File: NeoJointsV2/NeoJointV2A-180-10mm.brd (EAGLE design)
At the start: 30.5 x 12.4 mm, 5 parts

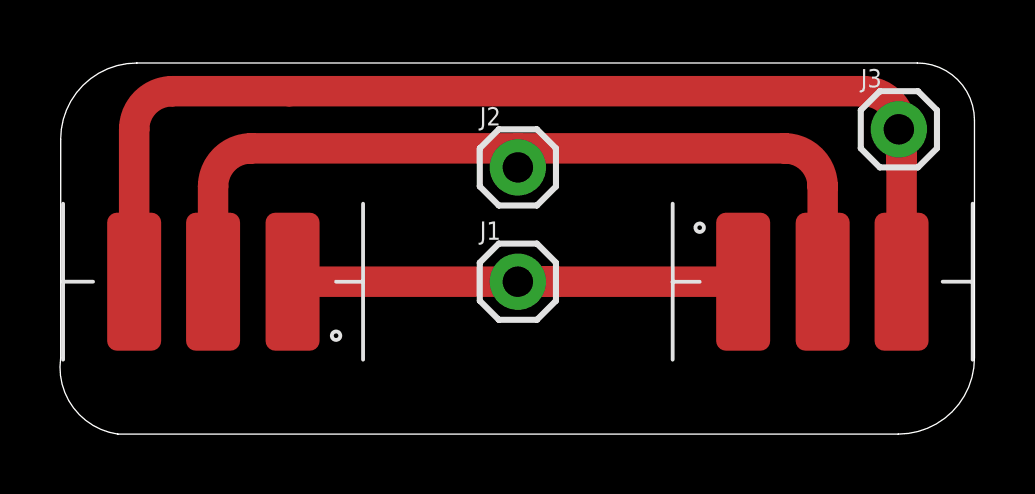
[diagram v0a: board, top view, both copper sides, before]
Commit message: added 180-degree variants
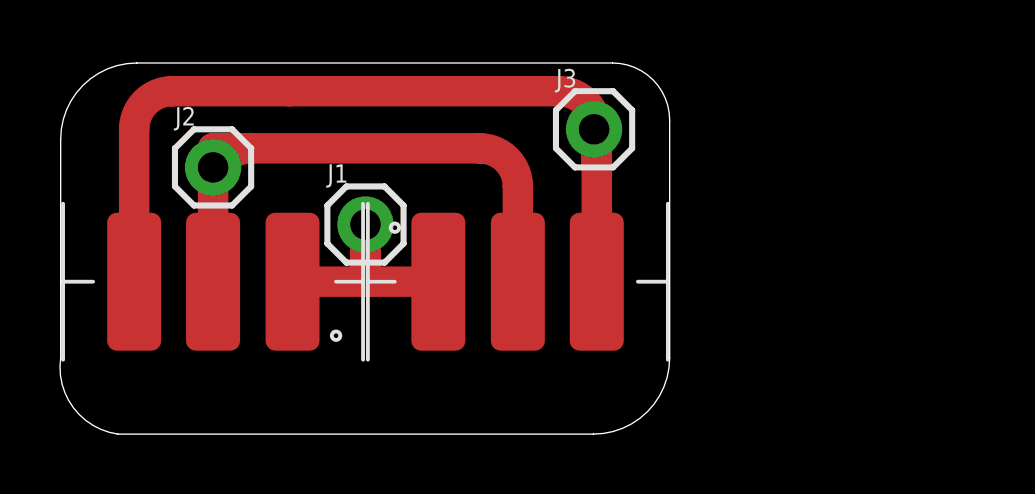
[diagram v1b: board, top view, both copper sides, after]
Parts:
- moved J2 10.2 mm to (5.08, 8.89)
- moved J3 10.2 mm to (17.8, 10.2)
- moved U$2 10.2 mm to (15.2, 5.08)
- moved J1 5.43 mm to (10.2, 6.99)
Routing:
- net N$3: track 38.1 -> 27.9 mm
- net N$1: track 16.3 -> 8.67 mm
- net N$2: track 28.4 -> 20.7 mm
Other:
- board size 30.5 x 12.4 mm -> 20.3 x 12.4 mm
- board text added: "J1"
- board text added: "J2"
- board text added: "J3"
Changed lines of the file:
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@@
 <layer number="123" name="tTestmark" color="7" fill="1" visible="no" active="yes"/>
 <layer number="124" name="bTestmark" color="7" fill="1" visible="no" active="yes"/>
-<layer number="125" name="_tNames" color="7" fill="1" visible="yes" active="yes"/>
+<layer number="125" name="_tNames" color="14" fill="1" visible="yes" active="yes"/>
 <layer number="126" name="_bNames" color="7" fill="1" visible="yes" active="yes"/>
 <layer number="127" name="_tValues" color="7" fill="1" visible="yes" active="yes"/>
@@
 <wire x1="0" y1="9.83" x2="0" y2="2.54" width="0" layer="20"/>
 <wire x1="0" y1="2.54" x2="1.905" y2="0" width="0" layer="20" curve="90"/>
-<wire x1="1.905" y1="0" x2="27.92" y2="0" width="0" layer="20"/>
-<wire x1="27.92" y1="0" x2="30.46" y2="2.54" width="0" layer="20" curve="90"/>
-<wire x1="30.46" y1="2.54" x2="30.46" y2="10.465" width="0" layer="20"/>
-<wire x1="30.46" y1="10.465" x2="28.555" y2="12.37" width="0" layer="20" curve="90"/>
-<wire x1="28.555" y1="12.37" x2="2.54" y2="12.37" width="0" layer="20"/>
+<wire x1="1.905" y1="0" x2="17.76" y2="0" width="0" layer="20"/>
+<wire x1="17.76" y1="0" x2="20.3" y2="2.54" width="0" layer="20" curve="90"/>
+<wire x1="20.3" y1="2.54" x2="20.3" y2="10.465" width="0" layer="20"/>
+<wire x1="20.3" y1="10.465" x2="18.395" y2="12.37" width="0" layer="20" curve="90"/>
+<wire x1="18.395" y1="12.37" x2="2.54" y2="12.37" width="0" layer="20"/>
 <wire x1="2.54" y1="12.37" x2="0" y2="9.83" width="0" layer="20" curve="90"/>
-<dimension x1="5.08" y1="8.56" x2="25.38" y2="8.56" x3="15.23" y3="13.335" textsize="0.6096" layer="48" width="0.0508" extwidth="0.1" visible="yes"/>
-<dimension x1="29.825" y1="12.37" x2="30.48" y2="0" x3="32.701696875" y3="6.185" textsize="0.6096" layer="48" dtype="vertical" width="0.0508" extwidth="0.1" visible="yes"/>
-<dimension x1="0" y1="11.43" x2="30.46" y2="11.43" x3="15.23" y3="15.875" textsize="0.6096" layer="48" dtype="horizontal" width="0.0508" extwidth="0.1" visible="yes"/>
+<dimension x1="5.08" y1="8.56" x2="15.22" y2="8.56" x3="10.15" y3="13.335" textsize="0.6096" layer="48" width="0.0508" extwidth="0.1" extlength="0.254" visible="yes"/>
+<dimension x1="19.665" y1="12.37" x2="20.32" y2="0" x3="22.541696875" y3="6.185" textsize="0.6096" layer="48" dtype="vertical" width="0.0508" extwidth="0.1" extlength="0.508" visible="yes"/>
+<dimension x1="0" y1="11.43" x2="20.3" y2="11.43" x3="10.15" y3="14.605" textsize="0.6096" layer="48" dtype="horizontal" width="0.0508" extwidth="0.1" extlength="0.508" visible="yes"/>
+<text x="8.89" y="8.382" size="0.6096" layer="125" ratio="20">J1</text>
+<text x="3.81" y="10.287" size="0.6096" layer="125" ratio="20">J2</text>
+<text x="16.51" y="11.557" size="0.6096" layer="125" ratio="20">J3</text>
 </plain>
 <attributes>
@@
 <elements>
 <element name="U$1" library="NeoJoints" package="LEDSTRIP-3P" value="LED_STRIP_3P" x="5.08" y="5.08" rot="R90"/>
-<element name="U$2" library="NeoJoints" package="LEDSTRIP-3P" value="LED_STRIP_3P" x="25.4" y="5.08" rot="R270"/>
-<element name="J1" library="SparkFun-Connectors" package="1X01" value="" x="15.24" y="5.08"/>
-<element name="J2" library="SparkFun-Connectors" package="1X01" value="" x="15.24" y="8.89"/>
-<element name="J3" library="SparkFun-Connectors" package="1X01" value="" x="27.94" y="10.16"/>
+<element name="U$2" library="NeoJoints" package="LEDSTRIP-3P" value="LED_STRIP_3P" x="15.24" y="5.08" rot="R270"/>
+<element name="J1" library="SparkFun-Connectors" package="1X01" value="" x="10.16" y="6.985"/>
+<element name="J2" library="SparkFun-Connectors" package="1X01" value="" x="5.08" y="8.89"/>
+<element name="J3" library="SparkFun-Connectors" package="1X01" value="" x="17.78" y="10.16"/>
 </elements>
 <signals>
@@
 <contactref element="U$2" pad="A"/>
 <contactref element="J1" pad="1"/>
-<wire x1="7.73" y1="5.08" x2="15.24" y2="5.08" width="1.016" layer="1"/>
-<wire x1="15.24" y1="5.08" x2="16.51" y2="5.08" width="1.016" layer="1"/>
-<wire x1="16.51" y1="5.08" x2="22.75" y2="5.08" width="1.016" layer="1"/>
-<wire x1="15.24" y1="5.08" x2="16.51" y2="5.08" width="1.016" layer="1"/>
+<wire x1="10.16" y1="6.985" x2="10.16" y2="5.08" width="1.016" layer="1"/>
+<wire x1="10.16" y1="5.08" x2="12.59" y2="5.08" width="1.016" layer="1"/>
+<wire x1="10.16" y1="6.985" x2="10.16" y2="5.08" width="1.016" layer="1"/>
+<wire x1="7.73" y1="5.08" x2="10.16" y2="5.08" width="1.016" layer="1"/>
 </signal>
 <signal name="N$2">
@@
 <wire x1="5.08" y1="5.08" x2="5.08" y2="8.255" width="1.016" layer="1"/>
 <wire x1="5.08" y1="8.255" x2="6.35" y2="9.525" width="1.016" layer="1" curve="-90"/>
-<wire x1="6.35" y1="9.525" x2="15.24" y2="9.525" width="1.016" layer="1"/>
-<wire x1="15.24" y1="9.525" x2="24.13" y2="9.525" width="1.016" layer="1"/>
-<wire x1="24.13" y1="9.525" x2="25.4" y2="8.255" width="1.016" layer="1" curve="-90"/>
-<wire x1="25.4" y1="8.255" x2="25.4" y2="5.08" width="1.016" layer="1"/>
-<wire x1="15.24" y1="8.89" x2="15.24" y2="9.525" width="1.016" layer="1"/>
+<wire x1="6.35" y1="9.525" x2="5.08" y2="9.525" width="1.016" layer="1"/>
+<wire x1="5.08" y1="9.525" x2="13.97" y2="9.525" width="1.016" layer="1"/>
+<wire x1="13.97" y1="9.525" x2="15.24" y2="8.255" width="1.016" layer="1" curve="-90"/>
+<wire x1="15.24" y1="8.255" x2="15.24" y2="5.08" width="1.016" layer="1"/>
+<wire x1="5.08" y1="8.89" x2="5.08" y2="9.525" width="1.016" layer="1"/>
 </signal>
 <signal name="N$3">
@@
 <wire x1="2.45" y1="10.16" x2="3.72" y2="11.43" width="1.016" layer="1" curve="-90"/>
 <wire x1="3.72" y1="11.43" x2="7.62" y2="11.43" width="1.016" layer="1"/>
-<wire x1="7.62" y1="11.43" x2="26.67" y2="11.43" width="1.016" layer="1"/>
-<wire x1="26.67" y1="11.43" x2="26.76" y2="11.43" width="1.016" layer="1"/>
-<wire x1="26.76" y1="11.43" x2="28.03" y2="10.16" width="1.016" layer="1" curve="-90"/>
-<wire x1="28.03" y1="10.16" x2="28.03" y2="8.89" width="1.016" layer="1"/>
-<wire x1="28.03" y1="8.89" x2="28.03" y2="5.08" width="1.016" layer="1"/>
-<wire x1="27.94" y1="10.16" x2="28.03" y2="10.07" width="1.016" layer="1" curve="-90"/>
-<wire x1="28.03" y1="10.07" x2="28.03" y2="8.89" width="1.016" layer="1"/>
+<wire x1="7.62" y1="11.43" x2="16.51" y2="11.43" width="1.016" layer="1"/>
+<wire x1="16.51" y1="11.43" x2="16.6" y2="11.43" width="1.016" layer="1"/>
+<wire x1="16.6" y1="11.43" x2="17.87" y2="10.16" width="1.016" layer="1" curve="-90"/>
+<wire x1="17.87" y1="10.16" x2="17.87" y2="8.89" width="1.016" layer="1"/>
+<wire x1="17.87" y1="8.89" x2="17.87" y2="5.08" width="1.016" layer="1"/>
+<wire x1="17.78" y1="10.16" x2="17.87" y2="10.07" width="1.016" layer="1" curve="-90"/>
+<wire x1="17.87" y1="10.07" x2="17.87" y2="8.89" width="1.016" layer="1"/>
 </signal>
 </signals>
